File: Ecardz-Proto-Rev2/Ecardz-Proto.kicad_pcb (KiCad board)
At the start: 4 copper layers, 53.2 x 93.2 mm, 106 parts, among them IC1 M24LR04E-RMN6T/2, J1 Conn_01x02, J2 Conn_01x24, J3 Conn_01x06, Q1 NMOS, U1 STM32L071K8Ux

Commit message: initial fit check for mech
final footprints defined and placement is mostly complete
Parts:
- removed the C8 at (51.8, -31.0)
- removed the C8 at (49.5, -23.0)
- removed the C8 at (40.5, -23.0)
- removed the C8 at (47.2, -23.0)
- removed the C8 at (40.2, -44.2)
- removed the C8 at (51.5, -44.2)
- removed the C8 at (36.0, -27.0)
- removed the C8 at (49.5, -27.0)
- removed the C8 at (47.2, -27.0)
- removed the C8 at (51.8, -27.0)
- removed the C8 at (51.0, -41.0)
- removed the C8 at (45.0, -27.0)
- removed the C8 at (35.8, -44.2)
- removed the C8 at (38.2, -31.0)
- removed the C8 at (42.8, -31.0)
- removed the C8 at (51.0, -36.5)
- removed the C8 at (42.8, -27.0)
- removed the C8 at (49.2, -44.2)
- removed the C8 at (40.5, -31.0)
- removed the C8 at (51.8, -23.0)
- removed the C8 at (36.0, -31.0)
- removed the C8 at (42.5, -44.2)
- removed the C8 at (45.0, -31.0)
- removed the C8 at (47.0, -44.2)
- removed the C8 at (44.8, -44.2)
- removed the C8 at (51.0, -38.8)
- removed the C8 at (49.5, -31.0)
- removed the C8 at (40.5, -27.0)
- removed the C8 at (45.0, -23.0)
- removed the C8 at (51.0, -34.2)
- removed the C8 at (33.8, -27.0)
- removed the C8 at (47.2, -31.0)
- removed the C8 at (38.2, -27.0)
- removed the C8 at (38.0, -44.2)
- removed the C8 at (42.8, -23.0)
- removed R18, R19: 0R, Resistor_SMD:R_0603_1608Metric_Pad0.98x0.95mm_HandSolder
- removed R23: DNP, Resistor_SMD:R_0603_1608Metric_Pad0.98x0.95mm_HandSolder
- removed TP7: TestPoint, TestPoint:TestPoint_Pad_2.0x2.0mm
- added C24: 11mF, SamacSys_Parts:CPH3225A, F.Cu at (480.9, 46.7)
- added C25: 11mF, SamacSys_Parts:CPH3225A, F.Cu at (466.2, 41.4)
- added C26: 11mF, SamacSys_Parts:CPH3225A, F.Cu at (477.7, 41.4)
- added C27: 11mF, SamacSys_Parts:CPH3225A, F.Cu at (458.7, 41.4)
- added C28: 11mF, SamacSys_Parts:CPH3225A, F.Cu at (473.4, 46.7)
- added C29: 11mF, SamacSys_Parts:CPH3225A, F.Cu at (477.2, 46.7)
- added C30: 11mF, SamacSys_Parts:CPH3225A, F.Cu at (481.5, 41.4)
- added C31: 11mF, SamacSys_Parts:CPH3225A, F.Cu at (455.0, 41.4)
- added C32: 11mF, SamacSys_Parts:CPH3225A, F.Cu at (451.2, 41.4)
- added C33: 11mF, SamacSys_Parts:CPH3225A, F.Cu at (469.7, 46.7)
- added C34: 11mF, SamacSys_Parts:CPH3225A, F.Cu at (462.5, 41.4)
- added C8: 200mF, SamacSys_Parts:RSCSK2043R3D01004T, F.Cu at (450.9, 51.2)
- added GND: TestPoint, TestPoint:TestPoint_Pad_D1.5mm, F.Cu at (448.9, 59.6)
- added J4: Conn_01x02, Connector_PinHeader_2.54mm:PinHeader_1x02_P2.54mm_Vertical, F.Cu at (475.9, 54.3)
- added J5: Conn_01x02, Connector_PinHeader_2.54mm:PinHeader_1x02_P2.54mm_Vertical, F.Cu at (444.4, 54.5)
- added Q2: Q_PMOS_GSD, Package_TO_SOT_SMD:SOT-23, F.Cu at (468.4, 25.8)
- added R20: 10k, Resistor_SMD:R_0603_1608Metric_Pad0.98x0.95mm_HandSolder, F.Cu at (439.7, 57.3)
- added R21: 10R, Resistor_SMD:R_0603_1608Metric_Pad0.98x0.95mm_HandSolder, F.Cu at (441.7, 54.5)
- added VDD: TestPoint, TestPoint:TestPoint_Pad_D1.5mm, F.Cu at (446.3, 59.6)
- C23: value TBD -> 11mF; footprint Capacitor_SMD:C_0805_2012Metric_Pad1.18x1.45mm_HandSolder -> SamacSys_Parts:CPH3225A
- R1: value 2.2R -> 0.47R
- R25: value 600R -> 0R
- R9: value 0R -> 10k
- moved H1 504.8 mm to (480.9, 70.9), turned to 180 degrees
- moved C11 481.5 mm to (481.9, 5.98), turned to -90 degrees
- moved D1 480.4 mm to (481.7, 1.23), turned to 90 degrees
- moved H2 478.5 mm to (480.9, -15.9), turned to 180 degrees
- moved D2 476.0 mm to (479.0, 7.58), turned to 90 degrees
- moved C13 475.8 mm to (479.4, 0.48), turned to -90 degrees
- moved L1 474.3 mm to (478.9, -5.02), turned to 180 degrees
- moved D3 472.4 mm to (477.5, 3.73), turned to 180 degrees
- moved Q1 469.8 mm to (476.4, 0.48), turned to 0 degrees
- moved C16 467.6 mm to (474.9, 5.98), turned to 180 degrees
- moved C1 467.4 mm to (474.4, 21.8)
- moved C2 464.0 mm to (472.7, 21.8)
- moved R4 463.6 mm to (473.4, -1.52), turned to 90 degrees
- moved C3 462.2 mm to (472.4, 3.23), turned to 180 degrees
- moved R1 462.0 mm to (472.4, 1.48), turned to 180 degrees
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- renumbered TP2 to CLK, TP3 to DIO, TP6 to GND, TP1 to NRST, TP5 to VDD
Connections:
- C14 pad 1: /NFC/NFC_BULK_CAP -> /NFC/V_E_HARVEST
- C22 pad 1: /NFC/NFC_BULK_CAP -> /NFC/V_E_HARVEST
- C5 pad 1: VDD -> /EINK/VCL
- J2 pad 10: VDD -> /EINK/VCL
- J2 pad 9: VDD -> /EINK/VCL
- L1 pad 2: VDD -> /EINK/VCL
- R2 pad 1: VDD -> /EINK/VCL
- R25 pad 1: Net-(R18-Pad2) -> /NFC/V_E_HARVEST
- R5 pad 1: VDD -> /NFC/VDD_NFC
- R6 pad 1: VDD -> /NFC/VDD_NFC
- R9 pad 1: /NFC/V_E_HARVEST -> VDD
- R9 pad 2: /NFC/NFC_BULK_CAP -> /EINK/EINK_POWER_CTRL_N
- U1 pad 14: unconnected-(U1-PB0-Pad14) -> /NFC/NFC_POWER
- U1 pad 9: unconnected-(U1-PA3-Pad9) -> /EINK/EINK_POWER_CTRL_N
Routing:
- net /EINK/D/C#: track 57.8 -> 17.5 mm
- net /EINK/CS#: track 52.3 -> 14.6 mm
- net /EINK/RES#: track 51.0 -> 16.7 mm
- net /EINK/BUSY: track 46.3 -> 12.9 mm
- net /EINK/SCL: track 40.6 -> 8.71 mm
- net /EINK/SDA: track 42.7 -> 13.4 mm
- net /NFC/V_E_HARVEST: track 26.0 -> 1.25 mm, vias 2 -> 1
- net /STM/I2C_NFC_SDA: track 27.6 -> 4.90 mm
- net /STM/I2C_NFC_SCL: track 27.9 -> 9.85 mm
- net VDD: track 40.9 -> 23.2 mm, vias 11 -> 7
- net /STM/NFC_BUSY: track 28.3 -> 11.4 mm
- net /STM/SWDIO: track 32.6 -> 21.0 mm
- net /STM/NRST: track 53.6 -> 42.1 mm
- net /STM/SWCLK: track 29.4 -> 17.9 mm
- net /STM/SWO: track 25.2 -> 13.7 mm
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- removed copper zone on B.Cu, net GND
- removed copper zone on F.Cu, net GND
- removed copper zone on In1.Cu, net GND
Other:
- board size 53.2 x 93.2 mm -> 52.5 x 92 mm
- board text added: "2"
- board text added: "A"
- board text added: "B"
- board text added: "For Instructional Use Only."
- board text added: "SOLIDWORKS Educational Product."
- board text removed: "CLK"
- board text removed: "DIO"
- board text removed: "GND"
- board text removed: "NRST"
- board text removed: "SWO"

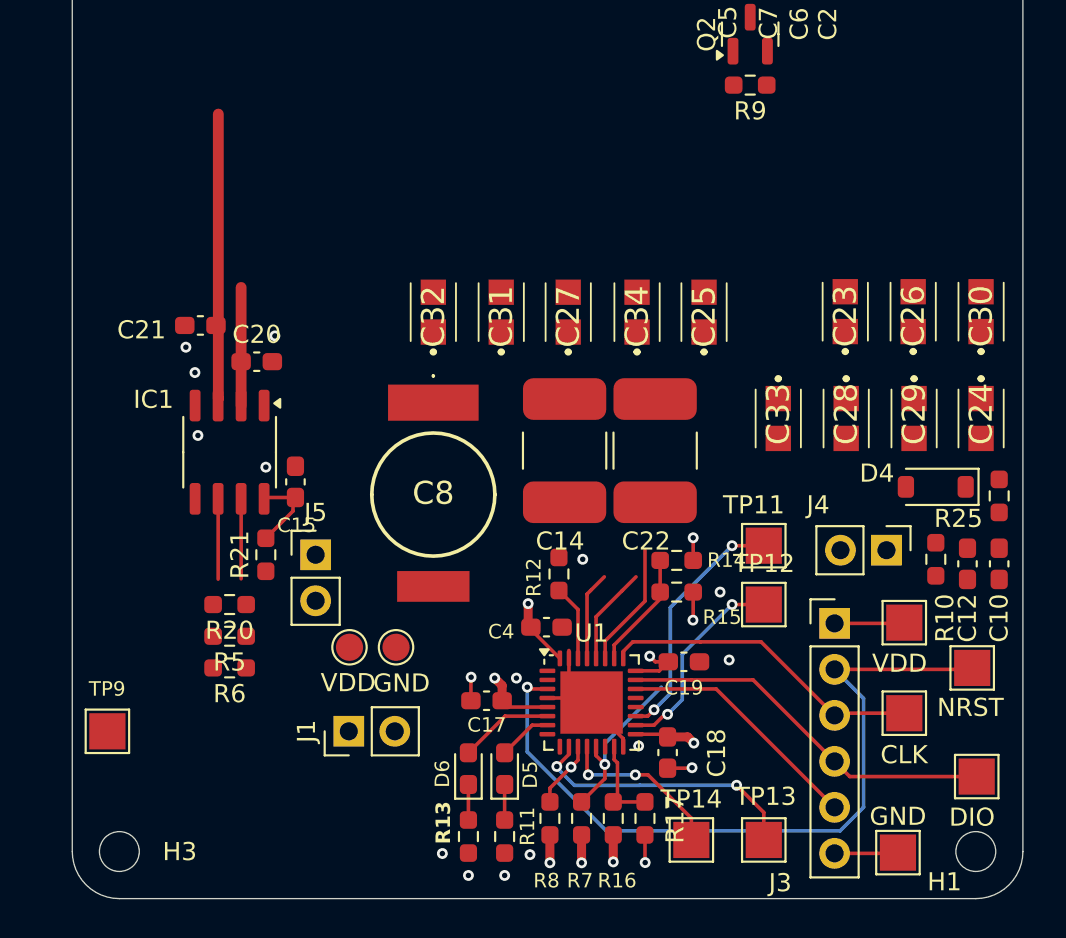
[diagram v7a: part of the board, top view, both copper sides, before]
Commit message: added antenna jumpers
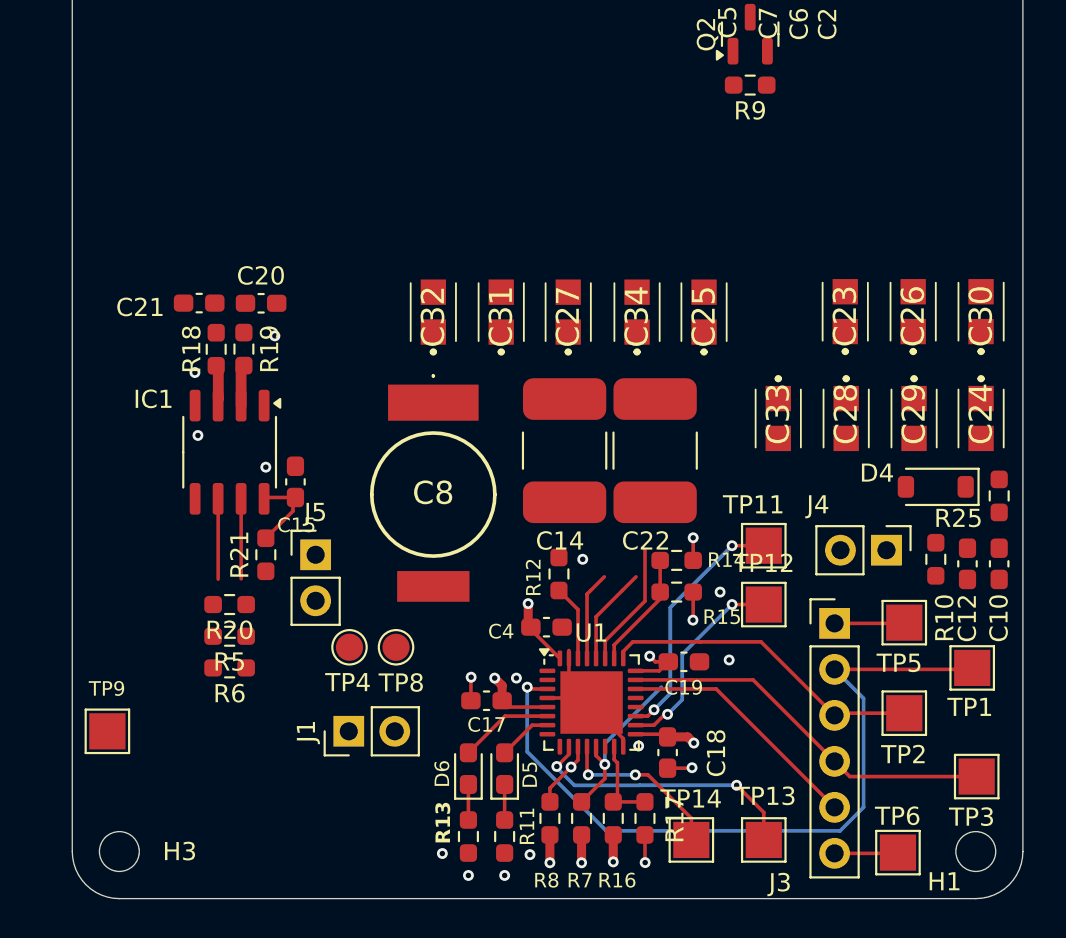
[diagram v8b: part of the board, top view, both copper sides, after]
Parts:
- added R18: 0R, Resistor_SMD:R_0603_1608Metric_Pad0.98x0.95mm_HandSolder, F.Cu at (438.9, 43.2)
- added R19: 0R, Resistor_SMD:R_0603_1608Metric_Pad0.98x0.95mm_HandSolder, F.Cu at (440.5, 43.1)
- moved C20 3.23 mm to (441.4, 40.6)
- moved C21 1.24 mm to (438.0, 40.6)
- renumbered NRST to TP1, CLK to TP2, DIO to TP3, VDD to TP4, VDD to TP5, GND to TP6, GND to TP8
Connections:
- C20 pad 1: Net-(IC1-AC0) -> Net-(C20-Pad1)
- C21 pad 1: Net-(IC1-AC0) -> Net-(C21-Pad1)
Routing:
- net Net-(IC1-AC0): track 1125.9 -> 1107.8 mm
- net GND: track 22.7 -> 22.6 mm, vias 22 -> 21
